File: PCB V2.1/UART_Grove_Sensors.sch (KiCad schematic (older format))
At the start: 11 parts, among them J5 B4B-PH-K-S(LF)(SN), J6 B4B-PH-K-S(LF)(SN), J7 B4B-PH-K-S(LF)(SN), J8 B4B-PH-K-S(LF)(SN), U4 74HC4052D

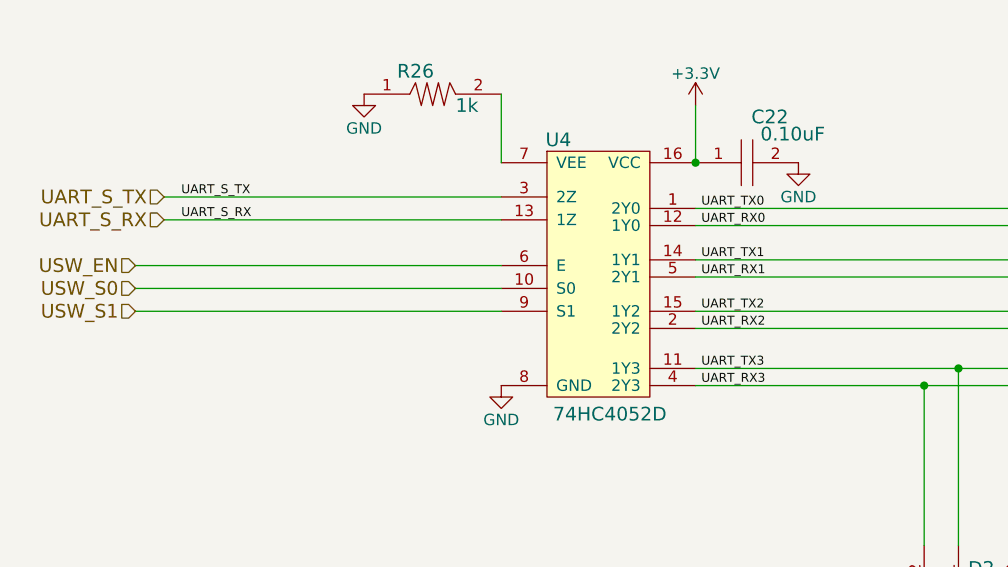
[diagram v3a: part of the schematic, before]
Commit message: 3D and Tweaks
3D files added for components for proper 3D rneder of the board. Board
tweaked, additional ground pours and sticking under neath the ESP-09,
cleaned up routign of JTAG , added labeling of all the pin signals.
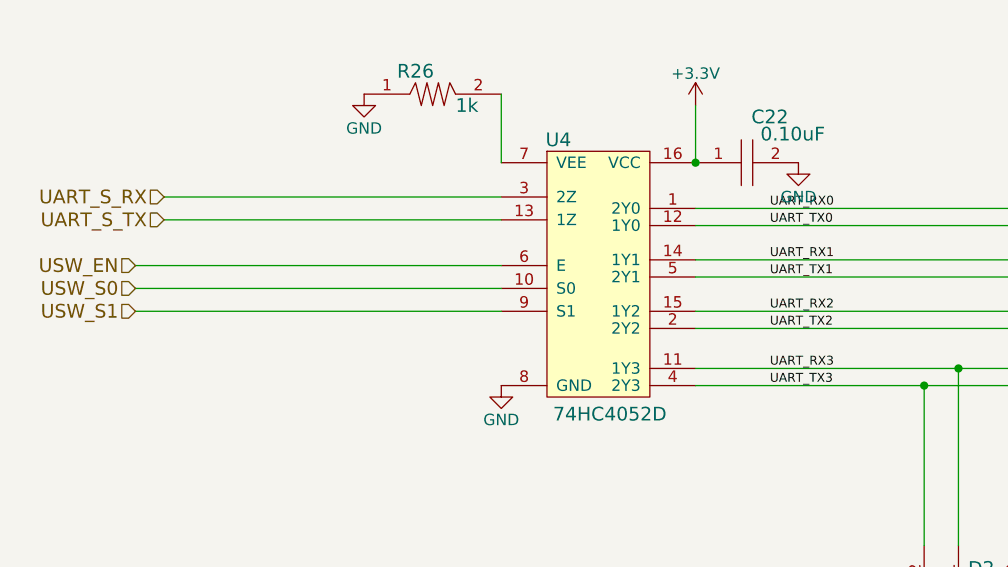
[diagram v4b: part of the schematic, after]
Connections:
- net UART_RX0: now also D5.1, J5.2, U4.1 (2Y0); no longer D5.2, J5.1, U4.12 (1Y0)
- net UART_RX1: now also D4.1, J6.2, U4.14 (1Y1); no longer D4.2, J6.1, U4.5 (2Y1)
- net UART_RX2: now also D3.1, J7.2, U4.15 (1Y2); no longer D3.2, J7.1, U4.2 (2Y2)
- net UART_RX3: now also D2.1, J8.2, U4.11 (1Y3); no longer D2.2, J8.1, U4.4 (2Y3)
- net UART_S_RX: now also U4.3 (2Z); no longer U4.13 (1Z)
- net UART_S_TX: now also U4.13 (1Z); no longer U4.3 (2Z)
- net UART_TX0: now also D5.2, J5.1, U4.12 (1Y0); no longer D5.1, J5.2, U4.1 (2Y0)
- net UART_TX1: now also D4.2, J6.1, U4.5 (2Y1); no longer D4.1, J6.2, U4.14 (1Y1)
- net UART_TX2: now also D3.2, J7.1, U4.2 (2Y2); no longer D3.1, J7.2, U4.15 (1Y2)
- net UART_TX3: now also D2.2, J8.1, U4.4 (2Y3); no longer D2.1, J8.2, U4.11 (1Y3)
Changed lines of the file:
@@
 Comment4 ""
 $EndDescr
+Text HLabel 1050 3975 0    60   Input ~ 0
+UART_S_TX
 Text HLabel 1050 3875 0    60   Input ~ 0
-UART_S_TX
-Text HLabel 1050 3975 0    60   Input ~ 0
 UART_S_RX
 Text HLabel 925  4175 0    60   Input ~ 0
@@
 $EndComp
 $Comp
-L GND #PWR42
+L GND #PWR43
 U 1 1 57D94298
 P 2525 4700
-F 0 "#PWR42" H 2525 4450 50  0001 C CNN
+F 0 "#PWR43" H 2525 4450 50  0001 C CNN
 F 1 "GND" H 2525 4550 50  0000 C CNN
 F 2 "" H 2525 4700 50  0000 C CNN
@@
 $EndComp
 $Comp
-L GND #PWR44
+L GND #PWR45
 U 1 1 57D9461A
 P 3825 3725
-F 0 "#PWR44" H 3825 3475 50  0001 C CNN
+F 0 "#PWR45" H 3825 3475 50  0001 C CNN
 F 1 "GND" H 3825 3575 50  0000 C CNN
 F 2 "" H 3825 3725 50  0000 C CNN
@@
 $EndComp
 $Comp
-L +3.3V #PWR43
+L +3.3V #PWR44
 U 1 1 57D94793
 P 3375 3475
-F 0 "#PWR43" H 3375 3325 50  0001 C CNN
+F 0 "#PWR44" H 3375 3325 50  0001 C CNN
 F 1 "+3.3V" H 3375 3615 50  0000 C CNN
 F 2 "" H 3375 3475 50  0000 C CNN
@@
 $EndComp
 $Comp
-L GND #PWR41
+L GND #PWR42
 U 1 1 57D94867
 P 1925 3425
-F 0 "#PWR41" H 1925 3175 50  0001 C CNN
+F 0 "#PWR42" H 1925 3175 50  0001 C CNN
 F 1 "GND" H 1925 3275 50  0000 C CNN
 F 2 "" H 1925 3425 50  0000 C CNN
@@
 $EndComp
 $Comp
-L +3.3V #PWR49
+L +3.3V #PWR50
 U 1 1 57D95562
 P 6400 3725
-F 0 "#PWR49" H 6400 3575 50  0001 C CNN
+F 0 "#PWR50" H 6400 3575 50  0001 C CNN
 F 1 "+3.3V" H 6400 3865 50  0000 C CNN
 F 2 "" H 6400 3725 50  0000 C CNN
@@
 $EndComp
 $Comp
-L +3.3V #PWR51
+L +3.3V #PWR52
 U 1 1 57D955D0
 P 7500 3975
-F 0 "#PWR51" H 7500 3825 50  0001 C CNN
+F 0 "#PWR52" H 7500 3825 50  0001 C CNN
 F 1 "+3.3V" H 7500 4115 50  0000 C CNN
 F 2 "" H 7500 3975 50  0000 C CNN
@@
 $EndComp
 $Comp
-L +3.3V #PWR53
+L +3.3V #PWR54
 U 1 1 57D955F6
 P 8500 4200
-F 0 "#PWR53" H 8500 4050 50  0001 C CNN
+F 0 "#PWR54" H 8500 4050 50  0001 C CNN
 F 1 "+3.3V" H 8500 4340 50  0000 C CNN
 F 2 "" H 8500 4200 50  0000 C CNN
@@
 $EndComp
 $Comp
-L +3.3V #PWR55
+L +3.3V #PWR56
 U 1 1 57D95640
 P 9500 4450
-F 0 "#PWR55" H 9500 4300 50  0001 C CNN
+F 0 "#PWR56" H 9500 4300 50  0001 C CNN
 F 1 "+3.3V" H 9500 4590 50  0000 C CNN
 F 2 "" H 9500 4450 50  0000 C CNN
@@
 $EndComp
 $Comp
-L GND #PWR50
+L GND #PWR51
 U 1 1 57D9573E
 P 6975 3525
-F 0 "#PWR50" H 6975 3275 50  0001 C CNN
+F 0 "#PWR51" H 6975 3275 50  0001 C CNN
 F 1 "GND" H 6975 3375 50  0000 C CNN
 F 2 "" H 6975 3525 50  0000 C CNN
@@
 $EndComp
 $Comp
-L GND #PWR52
+L GND #PWR53
 U 1 1 57D959DA
 P 7750 3725
-F 0 "#PWR52" H 7750 3475 50  0001 C CNN
+F 0 "#PWR53" H 7750 3475 50  0001 C CNN
 F 1 "GND" H 7750 3575 50  0000 C CNN
 F 2 "" H 7750 3725 50  0000 C CNN
@@
 $EndComp
 $Comp
-L GND #PWR54
+L GND #PWR55
 U 1 1 57D95B46
 P 8775 3975
-F 0 "#PWR54" H 8775 3725 50  0001 C CNN
+F 0 "#PWR55" H 8775 3725 50  0001 C CNN
 F 1 "GND" H 8775 3825 50  0000 C CNN
 F 2 "" H 8775 3975 50  0000 C CNN
@@
 $EndComp
 $Comp
-L GND #PWR45
+L GND #PWR46
 U 1 1 57D97A54
 P 4450 5925
-F 0 "#PWR45" H 4450 5675 50  0001 C CNN
+F 0 "#PWR46" H 4450 5675 50  0001 C CNN
 F 1 "GND" H 4450 5775 50  0000 C CNN
 F 2 "" H 4450 5925 50  0000 C CNN
@@
 $EndComp
 $Comp
-L GND #PWR46
+L GND #PWR47
 U 1 1 57D97BE5
 P 4875 5925
-F 0 "#PWR46" H 4875 5675 50  0001 C CNN
+F 0 "#PWR47" H 4875 5675 50  0001 C CNN
 F 1 "GND" H 4875 5775 50  0000 C CNN
 F 2 "" H 4875 5925 50  0000 C CNN
@@
 $EndComp
 $Comp
-L GND #PWR47
+L GND #PWR48
 U 1 1 57D97C1D
 P 5275 5925
-F 0 "#PWR47" H 5275 5675 50  0001 C CNN
+F 0 "#PWR48" H 5275 5675 50  0001 C CNN
 F 1 "GND" H 5275 5775 50  0000 C CNN
 F 2 "" H 5275 5925 50  0000 C CNN
@@
 $EndComp
 $Comp
-L GND #PWR48
+L GND #PWR49
 U 1 1 57D97C55
 P 5675 5925
-F 0 "#PWR48" H 5675 5675 50  0001 C CNN
+F 0 "#PWR49" H 5675 5675 50  0001 C CNN
 F 1 "GND" H 5675 5775 50  0000 C CNN
 F 2 "" H 5675 5925 50  0000 C CNN
@@
 $EndComp
 $Comp
-L GND #PWR56
+L GND #PWR57
 U 1 1 57D98002
 P 9750 4200
-F 0 "#PWR56" H 9750 3950 50  0001 C CNN
+F 0 "#PWR57" H 9750 3950 50  0001 C CNN
 F 1 "GND" H 9750 4050 50  0000 C CNN
 F 2 "" H 9750 4200 50  0000 C CNN
@@
 Text Notes 4175 1825 0    197  ~ 39
 UART Grove Sensors
-Text Label 3400 3925 0    39   ~ 0
+Text Label 3700 4000 0    39   ~ 0
 UART_TX0
-Text Label 3400 4000 0    39   ~ 0
+Text Label 3700 3925 0    39   ~ 0
 UART_RX0
-Text Label 3400 4150 0    39   ~ 0
+Text Label 3700 4225 0    39   ~ 0
 UART_TX1
-Text Label 3400 4225 0    39   ~ 0
+Text Label 3700 4150 0    39   ~ 0
 UART_RX1
-Text Label 3400 4375 0    39   ~ 0
+Text Label 3700 4450 0    39   ~ 0
 UART_TX2
-Text Label 3400 4450 0    39   ~ 0
+Text Label 3700 4375 0    39   ~ 0
 UART_RX2
-Text Label 3400 4700 0    39   ~ 0
+Text Label 3700 4625 0    39   ~ 0
 UART_RX3
-Text Label 3400 4625 0    39   ~ 0
+Text Label 3700 4700 0    39   ~ 0
 UART_TX3
 $Comp
@@
 	-1   0    0    1
 $EndComp
-Text Label 1125 3875 0    39   ~ 0
-UART_S_TX
-Text Label 1125 3975 0    39   ~ 0
-UART_S_RX
 Wire Wire Line
 	3375 3925 6875 3925
